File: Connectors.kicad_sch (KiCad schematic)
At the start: 8 parts, among them J1 282834-2

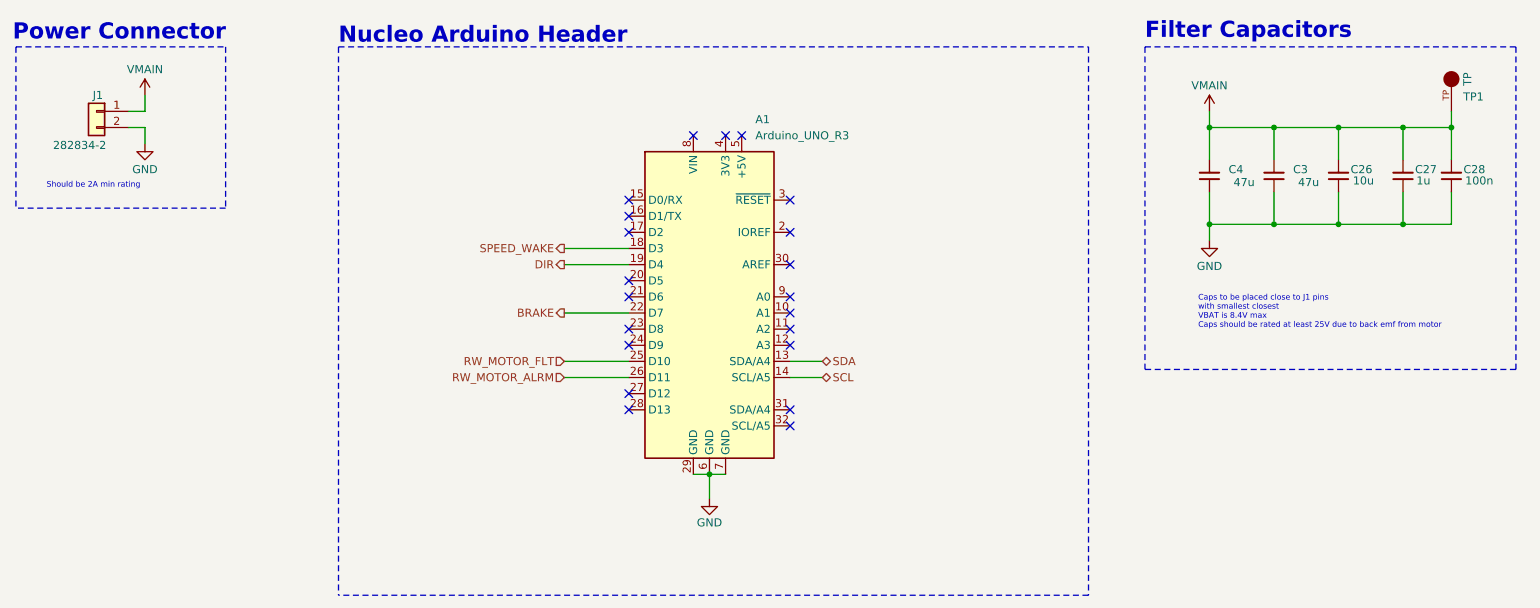
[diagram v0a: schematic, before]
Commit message: moved inductor and added leds
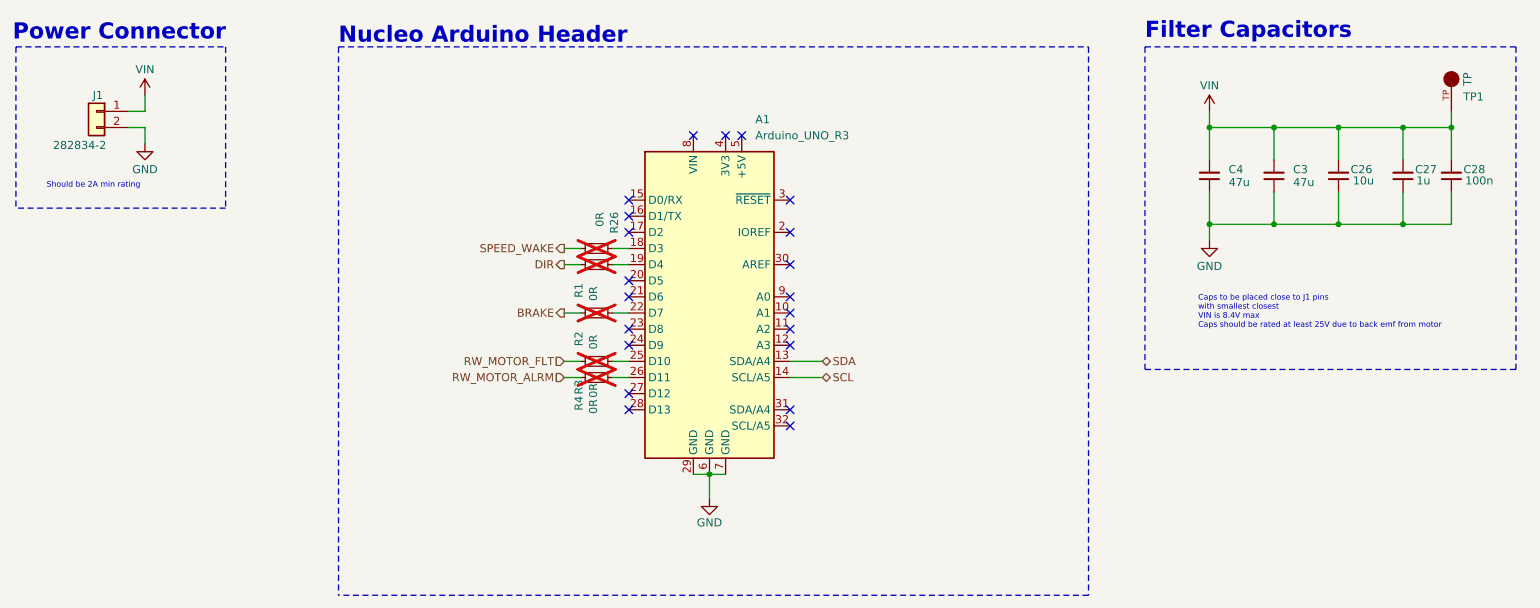
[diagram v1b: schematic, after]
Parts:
- added R1, R2, R26, R3, R4: 0R, Resistor_SMD:R_0402_1005Metric_Pad0.72x0.64mm_HandSolder, symbol Device:R_Small
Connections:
- net BRAKE: now also R2.2; no longer A1.22 (D7)
- net DIR: now also R1.2; no longer A1.19 (D4)
- net RW_MOTOR_ALRM: now also R4.2; no longer A1.26 (D11)
- net RW_MOTOR_FLT: now also R3.2; no longer A1.25 (D10)
- net SPEED_WAKE: now also R26.1; no longer A1.18 (D3)
- net VMAIN renamed VIN
- new net: A1.18 (D3), R26.2
- new net: A1.19 (D4), R1.1
- new net: A1.22 (D7), R2.1
- new net: A1.25 (D10), R3.1
- new net: A1.26 (D11), R4.1
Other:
- note added: "Caps to be placed close to J1 pins with smallest closest VIN is 8.4V max Caps should be rated at least 25V due to back emf from motor"
- note removed: "Caps to be placed close to J1 pins with smallest closest VBAT is 8.4V max Caps should be rated at least 25V due to back emf from motor"

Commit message: finished board
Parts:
- added R6, R7: 4.7k, Resistor_SMD:R_0603_1608Metric, symbol Device:R
- C28: footprint Capacitor_SMD:C_0402_1005Metric_Pad0.74x0.62mm_HandSolder -> Capacitor_SMD:C_0603_1608Metric
- R1, R2, R26, R3, R4: footprint Resistor_SMD:R_0402_1005Metric_Pad0.72x0.64mm_HandSolder -> Resistor_SMD:R_0603_1608Metric
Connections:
- net SCL: now also R7.1
- net SDA: now also R6.1
- net 3V3: now reaches A1.4 (3V3)
- net 3V3: now also R6.2, R7.2
- no-connect marks 21 -> 20
